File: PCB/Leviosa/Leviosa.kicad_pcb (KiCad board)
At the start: 2 copper layers, 80 x 80 mm, 49 parts, among them J1 2.54mm 1x03 Servo 1, J2 2.54mm 1x03 Servo 1, J3 2.54mm 1x03 Spare, J4 Barrel_Jack, Q3 TIP122, Q4 TIP122, U1 LM324, U2 ATtiny13A-P, U3 TPS1H200AQDGNRQ1, U5 L7805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

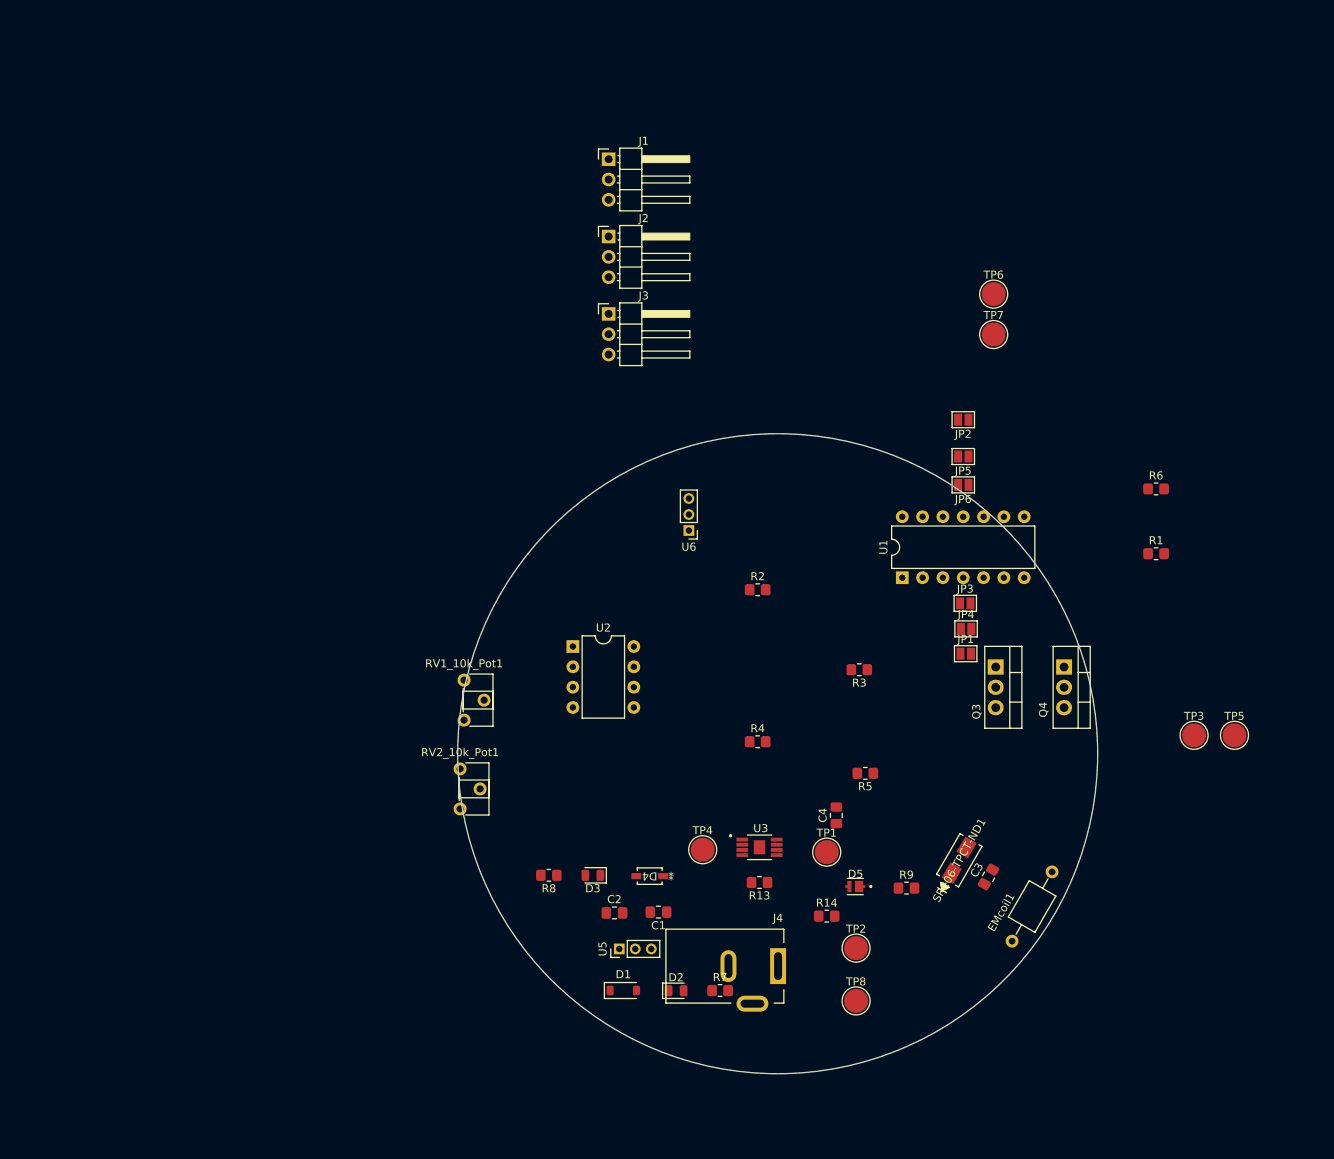
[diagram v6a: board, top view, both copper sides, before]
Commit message: update footprint copper layers
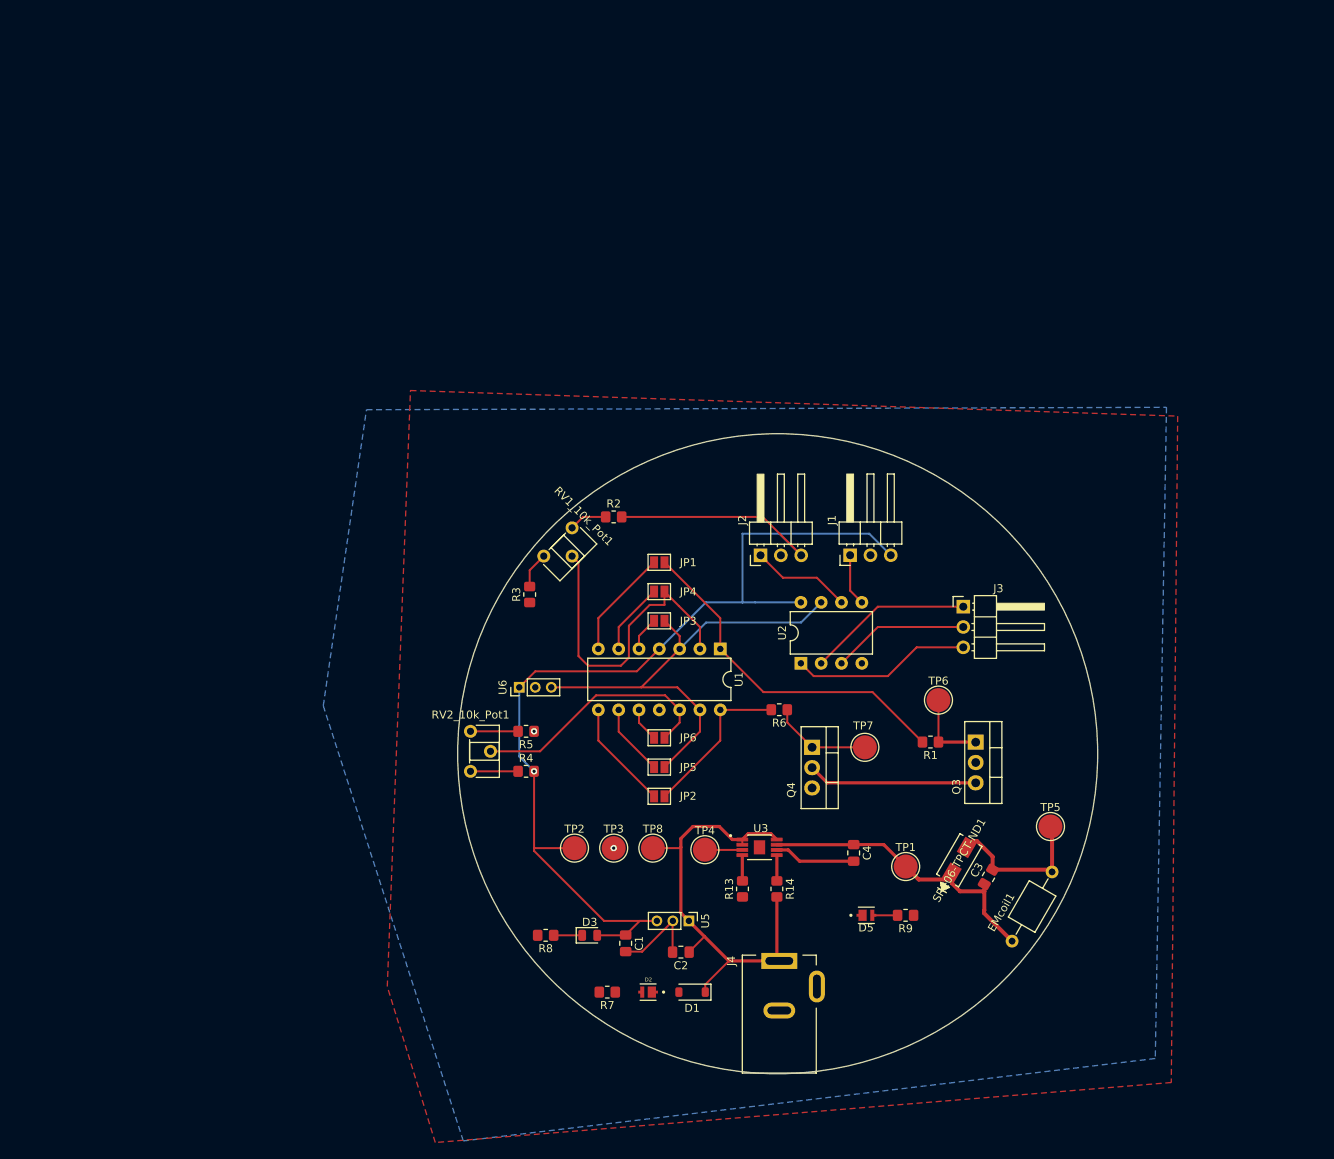
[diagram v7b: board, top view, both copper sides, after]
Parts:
- removed D4: D_Zener, SZMMSZ4679T1G:SOD-123_ONS
- D2: footprint LED_SMD:LED_0805_2012Metric -> MP-2016-1100-50-70:LED_MP-2016-1100-50-70
- moved TP3 73.9 mm to (139.5, 131.8)
- moved JP2 60.5 mm to (145.2, 125.3), turned to 0 degrees
- moved J1 58.0 mm to (169.1, 95.2), turned to 90 degrees
- moved J3 57.5 mm to (183.2, 101.6)
- moved R6 54.6 mm to (160.2, 114.5), turned to 180 degrees
- moved JP5 54.3 mm to (145.2, 121.7), turned to 0 degrees
- moved TP7 54.1 mm to (170.9, 119.2)
- moved TP6 51.2 mm to (180.1, 113.3)
- moved JP6 49.4 mm to (145.2, 118.0), turned to 0 degrees
- moved J2 44.1 mm to (157.9, 95.2), turned to 90 degrees
- moved R5 42.7 mm to (128.6, 117.2)
- moved R3 42.3 mm to (129.0, 100.1), turned to 90 degrees
- moved JP1 40.0 mm to (145.2, 96.1), turned to 180 degrees
- moved JP4 38.6 mm to (145.2, 99.7), turned to 180 degrees
- moved JP3 38.3 mm to (145.2, 103.4), turned to 180 degrees
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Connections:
- D3 pad 1: (no net) -> Net-(D3-K)
- D3 pad 2: (no net) -> /5V
- R8 pad 1: Net-(D3-PadC) -> Net-(D3-K)
- RV1_10k_Pot1 pad 1: Net-(R3-Pad2) -> Net-(R2-Pad1)
- RV1_10k_Pot1 pad 3: Net-(R2-Pad1) -> Net-(R3-Pad2)
- RV2_10k_Pot1 pad 1: Net-(R4-Pad1) -> Net-(R5-Pad2)
- RV2_10k_Pot1 pad 3: Net-(R5-Pad2) -> Net-(R4-Pad1)
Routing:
- net /5V: track 0.00 -> 149.5 mm, vias 0 -> 1
- net /PB2: track 0.00 -> 59.9 mm
- net +12V: track 0.00 -> 58.1 mm
- net /set_point_trigger: track 0.00 -> 43.8 mm
- net /set_point: track 0.00 -> 40.5 mm
- net /V_out: track 0.00 -> 38.4 mm
- net /no_magnet_point: track 0.00 -> 31.6 mm
- net /PB5: track 0.00 -> 22.5 mm
- net GND: track 0.00 -> 21.6 mm, vias 0 -> 2
- net /transistor1_output: track 0.00 -> 21.2 mm
- net /PB3: track 0.00 -> 20.7 mm
- net /no_magnet_point_trigger: track 0.00 -> 20.1 mm
- net /coil_output: track 0.00 -> 19.3 mm
- net /PB4: track 0.00 -> 17.1 mm
- net /spare_set_point_trigger: track 0.00 -> 13.7 mm
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- added copper zone on B.Cu, net GND
- added copper zone on F.Cu, net GND

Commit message: Update PCB
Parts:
- Schottky1: renamed from SR206-TPCT-ND1; value Schottky Diode -> Schottky Diode SR206-TPCT-ND1
- moved J4 1.63 mm to (159.9, 144.3)
- renumbered EMcoil1 to Coil1, RV1_10k_Pot1 to Pot1, RV2_10k_Pot1 to Pot2
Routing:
- net +12V: track 58.1 -> 56.4 mm
